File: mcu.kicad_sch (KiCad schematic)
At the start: 9 parts, among them J1 BOOT SEL, SW1 Reset Switch, U2 STM32F030F4Px

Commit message: fix(connector): correct J1 footprint to 1x03 to match symbol
BOOT SEL jumper would not assemble with a 2-pin footprint.
J1 now uses PinHeader_1x03 to match its 3-pin Conn_01x03 symbol.
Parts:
- J1: footprint Connector_PinHeader_2.54mm:PinHeader_1x02_P2.54mm_Horizontal -> Connector_PinHeader_2.54mm:PinHeader_1x03_P2.54mm_Vertical
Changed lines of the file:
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@@
 			)
 		)
-		(property "Footprint" "Connector_PinHeader_2.54mm:PinHeader_1x02_P2.54mm_Horizontal"
+		(property "Footprint" "Connector_PinHeader_2.54mm:PinHeader_1x03_P2.54mm_Vertical"
 			(at 213.36 38.1 0)
 			(hide yes)

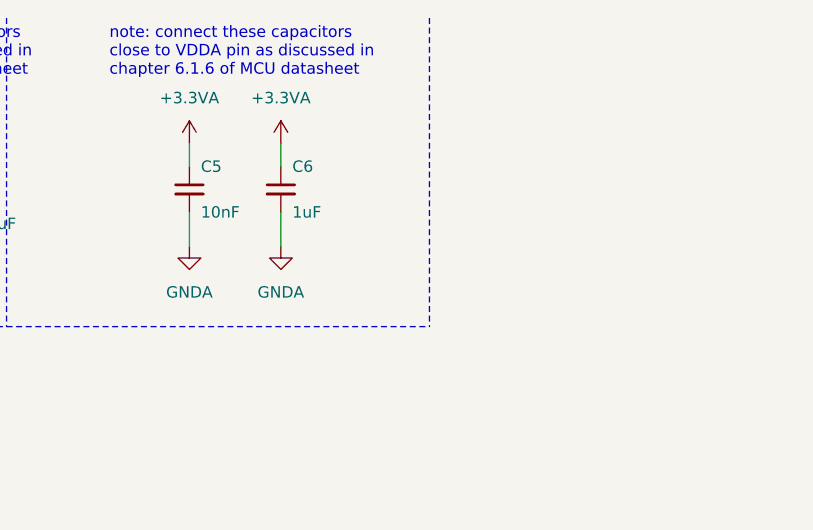
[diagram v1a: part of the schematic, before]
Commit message: fix(ground): tie GNDA to GND with 0R star point
Analog ground island (C5/C6 bottom plates plus FT232RL AGND) was
floating with no reference to system ground. Adds R12 0R 0603 on
the MCU sheet as a single-point tie, keeping GNDA/GND as separate
nets for ERC while giving the analog reference a defined return.
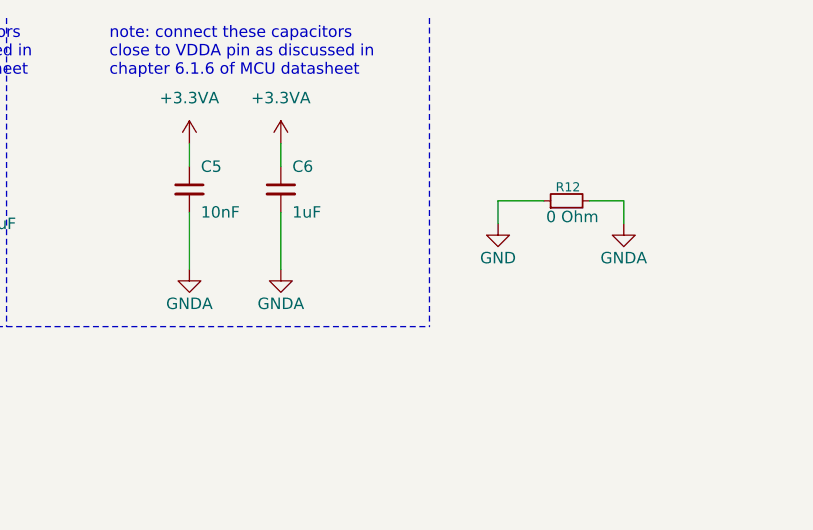
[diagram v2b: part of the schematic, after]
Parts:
- added R12: 0 Ohm, Resistor_SMD:R_0603_1608Metric_Pad0.98x0.95mm_HandSolder, symbol Device:R_Small
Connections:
- net GND: now also R12.1
- net GNDA: now also R12.2

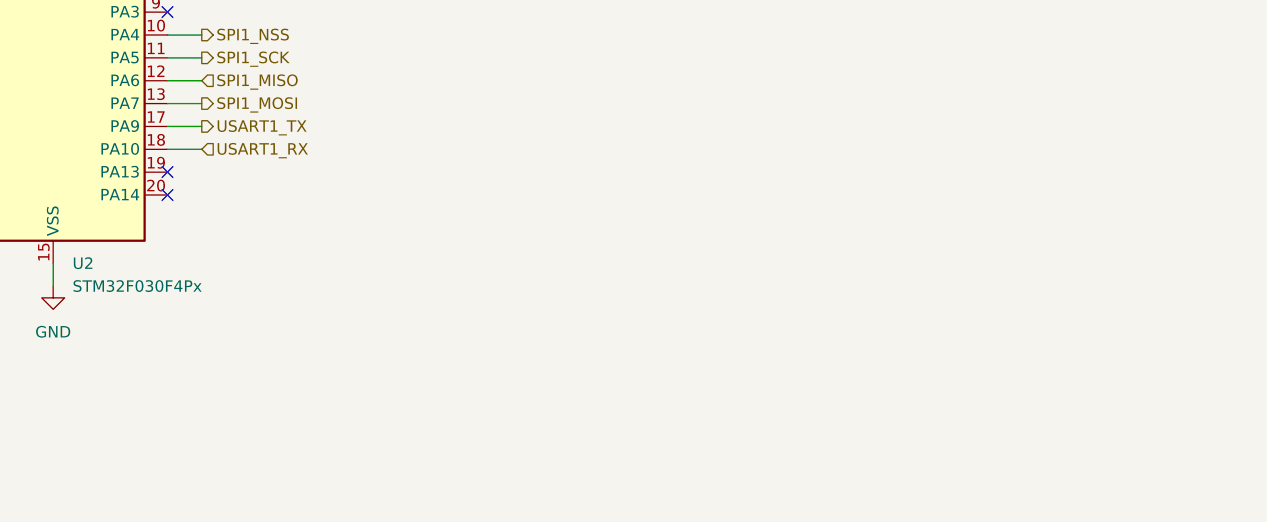
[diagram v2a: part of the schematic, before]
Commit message: fix(mcu): add SWD programming header for PA13/PA14
PA13/SWDIO and PA14/SWCLK were flagged no-connect, leaving no
debug or programming path after assembly. Adds J4 1x04 header
with +3.3V, SWCLK, SWDIO and GND for ST-Link programming and
bring-up debug.
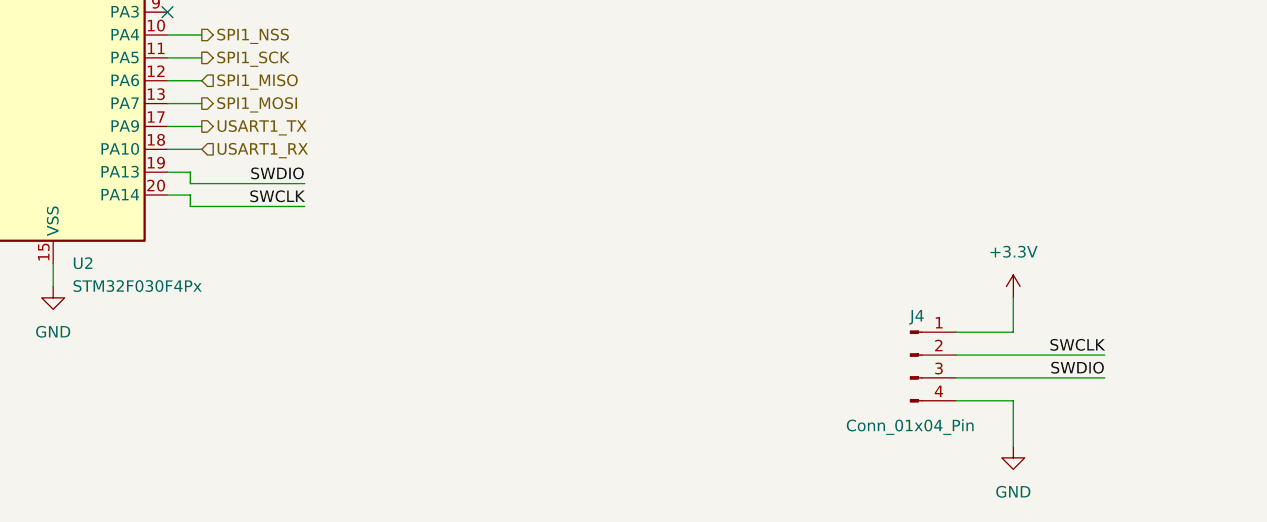
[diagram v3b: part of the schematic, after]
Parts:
- added J4: Conn_01x04_Pin, Connector_PinHeader_2.54mm:PinHeader_1x04_P2.54mm_Vertical, symbol Connector:Conn_01x04_Pin
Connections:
- net +3.3V: now also J4.1 (Pin_1)
- net GND: now also J4.4 (Pin_4)
- net SWDIO: now reaches U2.19 (PA13)
- net SWDIO: now also J4.3 (Pin_3)
- net SWCLK: now reaches U2.20 (PA14)
- net SWCLK: now also J4.2 (Pin_2)
- no-connect marks 9 -> 7
